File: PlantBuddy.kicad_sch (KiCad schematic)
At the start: 71 parts, among them J1 USB_C_Receptacle_USB2.0, J101 JST, J102 J-Link SWD, J4 External, Q101 DMG1012T, SW1 SW_Push, U1 LTR-303ALS-01, U101 RT9080-33GJ5, U102 nRF52832-QFAA, U104 XB5350A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

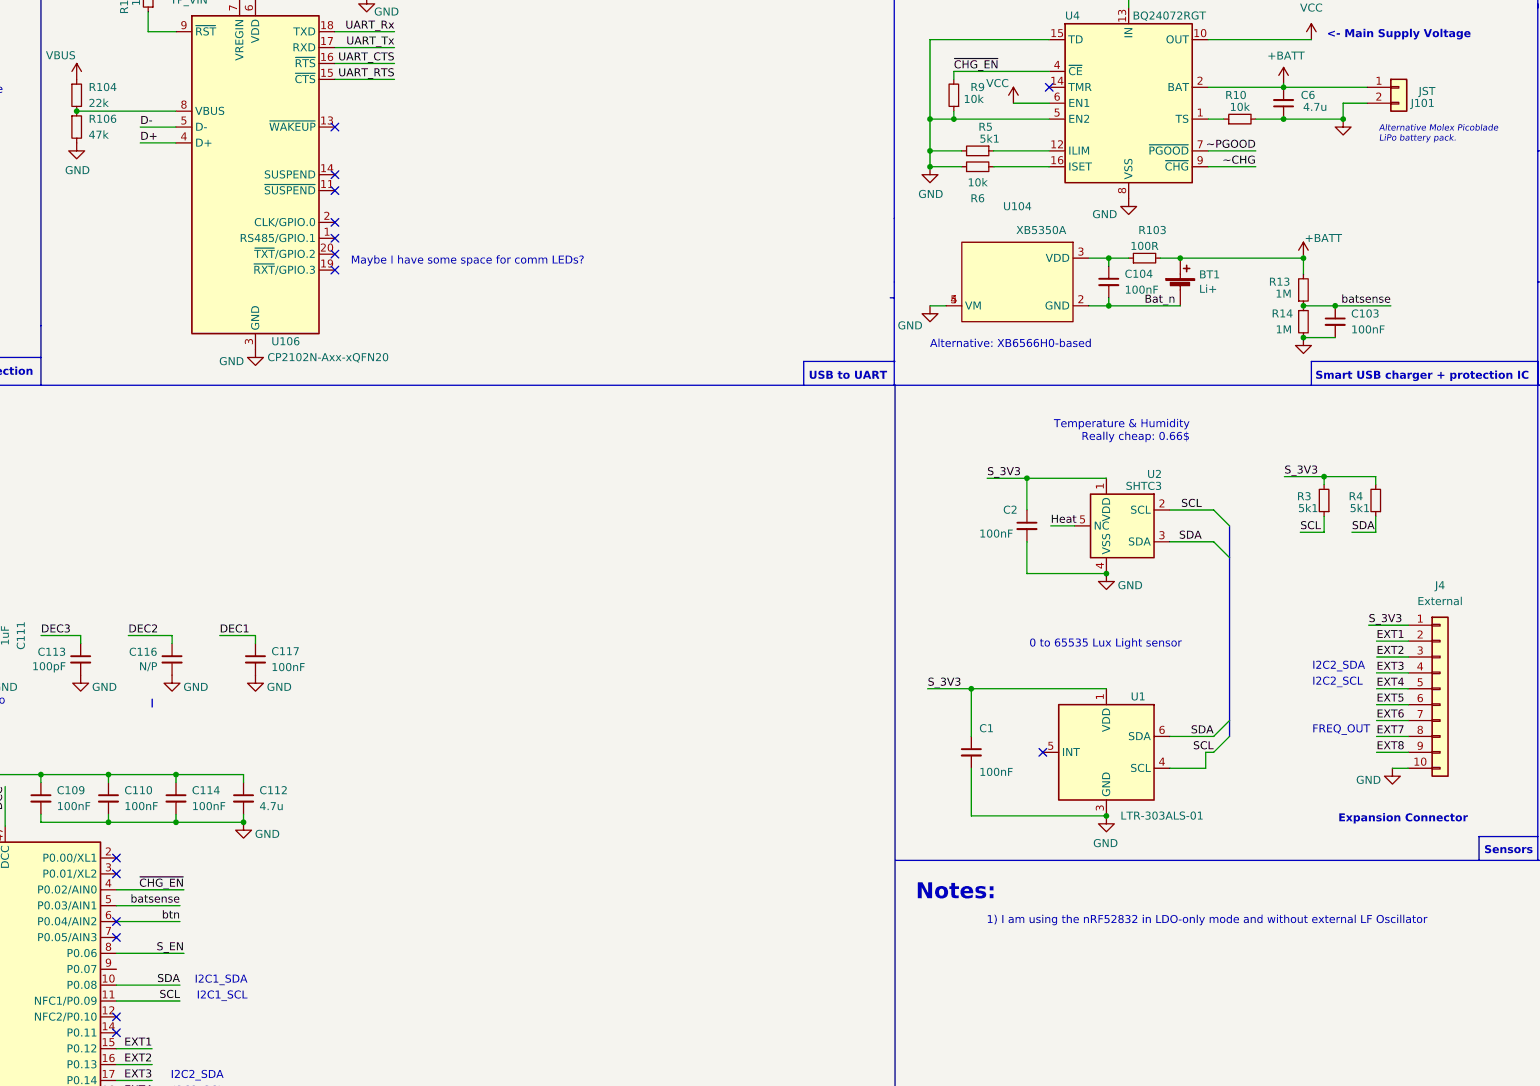
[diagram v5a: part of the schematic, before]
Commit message: Last order before main order. NO MORE ORDERS ALLOWED
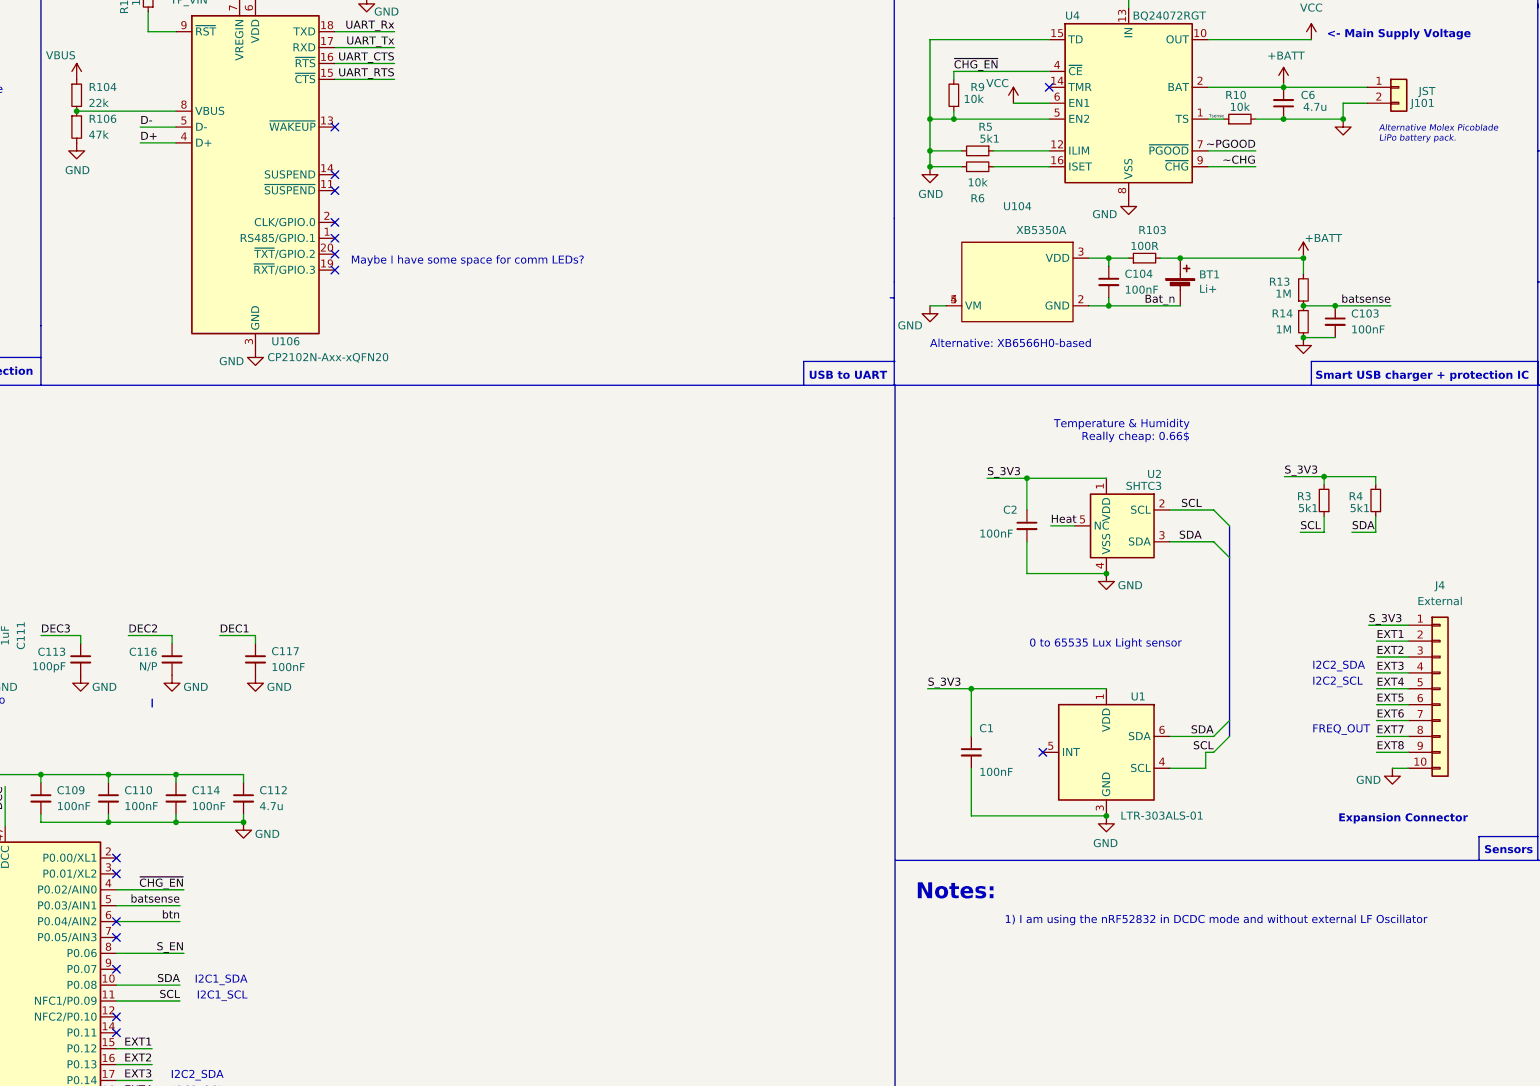
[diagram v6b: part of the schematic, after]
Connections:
- net Tsense: now reaches R10.1, U4.1 (TS)
- no-connect marks 27 -> 28
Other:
- note added: "1) I am using the nRF52832 in DCDC mode and without external LF Oscillator"
- note removed: "1) I am using the nRF52832 in LDO-only mode and without external LF Oscillator"
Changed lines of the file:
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@@
   (no_connect (at 162.56 66.675))
   (no_connect (at 387.223 116.586))
+  (no_connect (at 127.635 178.435))
   (no_connect (at 162.56 43.815))
   (no_connect (at 162.56 51.435))
@@
     (effects (font (size 1.27 1.27)) (justify left bottom))
   )
-  (text "1) I am using the nRF52832 in LDO-only mode and without external LF Oscillator"
+  (text "1) I am using the nRF52832 in DCDC mode and without external LF Oscillator"
     (at 337.185 171.45 0)
     (effects (font (size 1.27 1.27)) (justify right bottom))
@@
     (effects (font (size 1.27 1.27)) (justify left bottom))
   )
+  (label "Tsense" (at 302.26 42.545 0)
+    (effects (font (size 0.5 0.5)) (justify left bottom))
+  )
   (label "UART_Tx" (at 137.795 224.155 180)

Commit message: Added voltage monitoring IC. Shuts everything down if Vbat < 3V
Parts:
- U105: value CN809R -> CN809T; LCSC C840519 -> C840520
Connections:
- net +3V3: no longer U105.3 (VCC)
- net VCC: now also U105.3 (VCC); no longer U5.3 (EN)
- net ~{tRST}: no longer U105.2 (~{RST})
- new net PWR_EN: U105.2 (~{RST}), U5.3 (EN)
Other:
- note added: "Reset circuit. 3.08V Push-pull"
- note removed: "Might not be needed because of the integrated Power On Reset circuit"
- note removed: "Reset circuit. 2.63V Push-pull"
- moved on the sheet: BT1, C10, C101, C103, C104, C11, C115, C5, C6, J101, R10, R101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

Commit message: Fixed high power consumption when Vsupply < 3V3
- Added 3V LDO instead of 3.3V LDO.
- Changed RGB LED from Neopixel to simple PWM-based.
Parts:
- removed D1: SK6812SMINI-ER, Neopixel:XL-3528RGBW-WS2812B, symbol neopixel:XL-3528RGBW-WS2812B
- removed Q101: DMG1012T, Package_TO_SOT_SMD:SOT-523, symbol Transistor_FET:DMG1012T
- added D102: LED_RGBA, LED_SMD:LED_Lumex_SML-LX0404SIUPGUSB, symbol Device:LED_RGBA
- added R107, R109: 120R, Resistor_SMD:R_0402_1005Metric, symbol Device:R_Small
- R102: value 10k -> 330R; LCSC C25744 -> C25104; MPN 0603WAF5101T5E -> (none)
- TP101: value TP_3V3 -> TP_3V0
- TP102: value TP_s3V3 -> TP_s3V0
- U101, U5: value RT9080-33GJ5 -> ME6231C33M5G; Details 3.3V 600mA LDO with 2uA Iq -> 3V 500mA LDO with 1uA Iq; LCSC C841192 -> C610253
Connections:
- net GND: no longer R102.1
- net LED_B: now reaches U102.29 (P0.24)
- net LED_B: now also R107.2
- net +3V3 renamed +3V0
- net +3V0: now also D102.4 (A)
- net EN_RGB renamed LED_G
- net LED_G: now also R109.2; no longer R102.2
- net LED_TX renamed LED_R
- net LED_R: now also R102.2
- net S_3V3 renamed S_3V0
- new net: D102.1 (RK), R102.1
- new net: D102.3 (BK), R107.1
- new net: D102.2 (GK), R109.1
- no-connect marks 28 -> 26
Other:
- note added: "1) The Riktek LDO doesn't like voltages below its output voltage. and starts to draw a lot of power if going below. Solutions: use a 3V LDO. Also change the Riktek with a more known brand."
- note added: "Findings:"
- note added: "For If = 3mA"
- note added: "Status LED."
- note removed: "Status LED. RGB Neopixel"
